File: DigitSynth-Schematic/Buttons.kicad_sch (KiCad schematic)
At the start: 12 parts

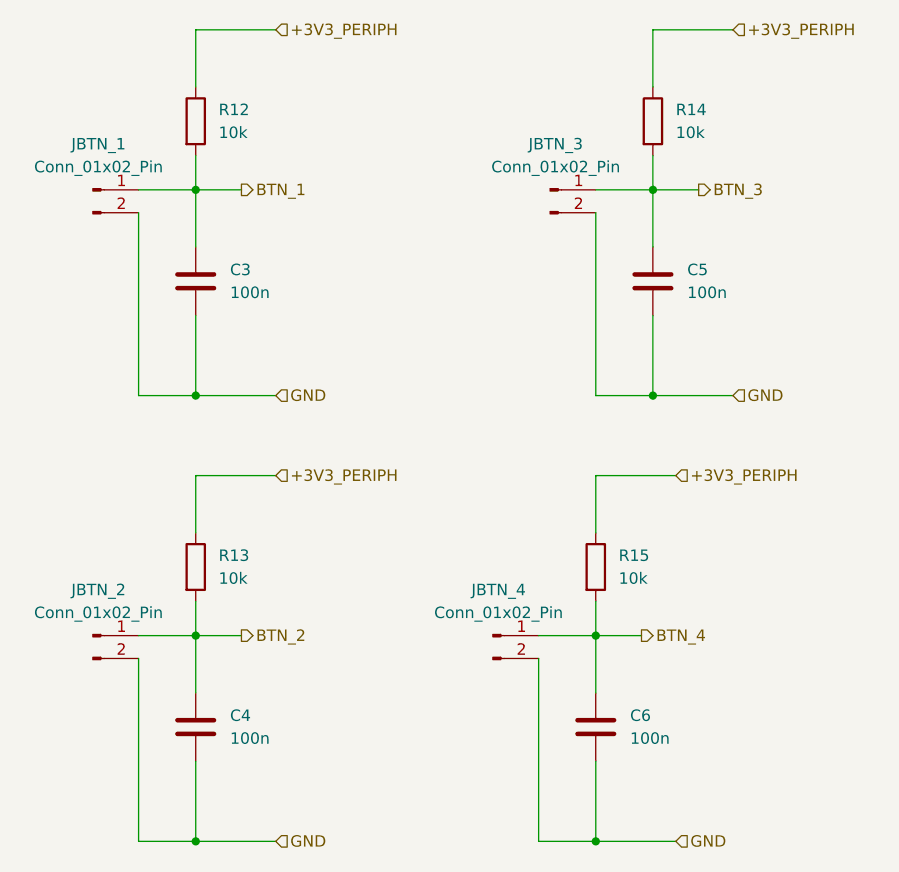
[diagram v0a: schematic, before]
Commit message: updated schematic for PCB design
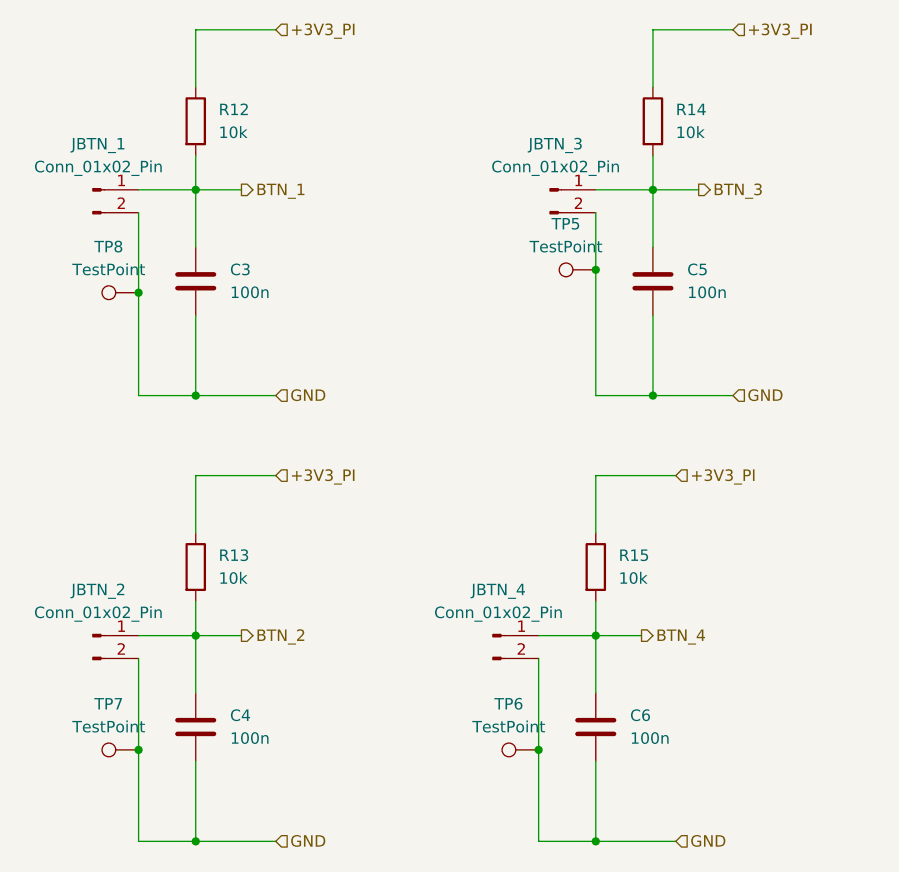
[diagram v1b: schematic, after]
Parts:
- added TP5, TP6, TP7, TP8: TestPoint, symbol Connector:TestPoint
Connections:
- net GND: now also TP5.1, TP6.1, TP7.1, TP8.1
- net +3V3_PERIPH renamed +3V3_PI
